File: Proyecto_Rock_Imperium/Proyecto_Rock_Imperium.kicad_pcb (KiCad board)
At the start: 2 copper layers, 53.3 x 58.4 mm, 19 parts, among them Q1 2N3904, Q2 2N3904

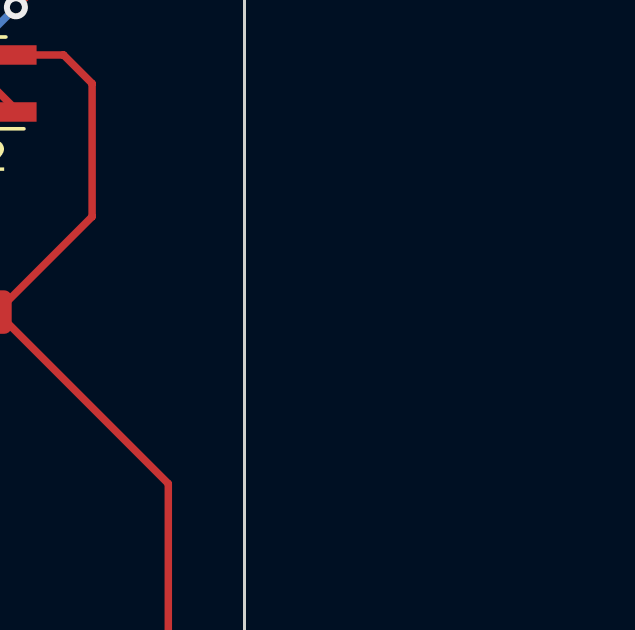
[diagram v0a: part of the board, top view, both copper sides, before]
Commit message: Actualizado esquema y añadido switch
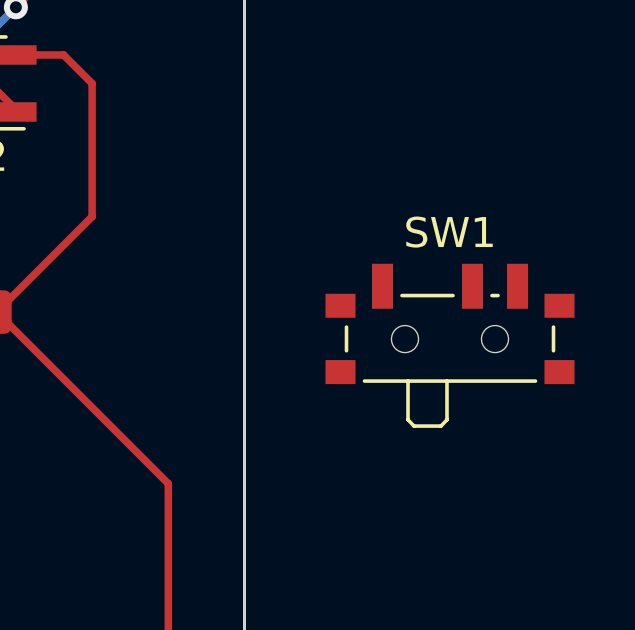
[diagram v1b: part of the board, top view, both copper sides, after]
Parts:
- added SW1: SW_SPDT, Button_Switch_SMD:SW_SPDT_PCM12, F.Cu at (171.9, 76.8)
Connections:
- net Net-(BT1--) renamed GND
- net Net-(D1-A) renamed /leds_b
- net Net-(D1-K) renamed /k_b
- net Net-(D4-A) renamed /leds_a
- net Net-(D4-K) renamed /k_a
- net Net-(Q1-B) renamed /chr_a
- net Net-(Q2-B) renamed /chr_b
- BT1 pad 1: Net-(BT1-+) -> +3V0
- R1 pad 1: Net-(BT1-+) -> /sw_on
- R2 pad 1: Net-(BT1-+) -> /sw_on
- R3 pad 1: Net-(BT1-+) -> /sw_on
- R4 pad 1: Net-(BT1-+) -> /sw_on
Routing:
- net Net-(BT1-+): track 99.8 -> 0.00 mm, vias 2 -> 0
- net (no net): track 0.00 -> 99.8 mm, vias 0 -> 2

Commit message: terminado a falta de revision
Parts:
- removed Ref**: Val**, proyecto_rock:RoCkImPeRiUm
- removed Ref**: Val**, proyecto_rock:IEEE2
- removed Ref**: Val**, proyecto_rock:UPCT2
- removed Ref**: Val**, proyecto_rock:UPCT
- added REF**: TestPoint_Pad_D4.0mm, TestPoint:TestPoint_Pad_D4.0mm, B.Cu at (156.0, 78.5)
- BT1, SW1: moved to B.Cu
- moved R3 71.5 mm to (178.5, 102.5), turned to 90 degrees
- moved Q1 70.8 mm to (190.4, 85.2), turned to 0 degrees
- moved BT1 51.8 mm to (155.9, 107.6), turned to 150 degrees
- moved R4 49.9 mm to (124.9, 97.3), turned to 90 degrees
- moved SW1 48.9 mm to (156.3, 123.2), turned to 180 degrees
- moved R2 42.8 mm to (172.0, 96.4), turned to 180 degrees
- moved D3 42.8 mm to (155.9, 116.1), turned to 0 degrees
- moved D4 42.0 mm to (166.2, 91.1)
- moved C1 39.6 mm to (190.0, 96.4), turned to 180 degrees
- moved D2 35.5 mm to (172.6, 82.1), turned to 180 degrees
- moved Q2 34.9 mm to (123.7, 81.2)
- moved R1 30.8 mm to (130.5, 97.4), turned to 90 degrees
- moved D1 22.8 mm to (140.9, 90.3)
- moved D6 22.3 mm to (172.6, 76.8), turned to 180 degrees
- moved C2 12.6 mm to (126.4, 87.5), turned to -90 degrees
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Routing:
- net (no net): track 99.8 -> 0.00 mm, vias 2 -> 0
- net /sw_on: track 0.00 -> 96.6 mm, vias 0 -> 2
- net /k_b: track 37.3 -> 111.2 mm, vias 0 -> 4
- net /chr_a: track 56.4 -> 122.4 mm
- net /leds_b: track 26.7 -> 80.1 mm, vias 0 -> 5
- net /chr_b: track 120.2 -> 75.4 mm, vias 0 -> 2
- net +3V0: track 0.00 -> 39.6 mm
- net /leds_a: track 26.7 -> 48.0 mm, vias 0 -> 4
- net /k_a: track 56.9 -> 73.6 mm, vias 2 -> 5
- net GND: track 44.6 -> 42.1 mm, vias 2 -> 1
- added copper zone on B.Cu, net GND
- added copper zone on F.Cu, net GND
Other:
- board size 53.3 x 58.4 mm -> 82.1 x 66.2 mm

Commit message: terminado. Pendiente revision y pulir bateria
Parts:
- moved C1 11.3 mm to (182.1, 88.3)
- moved C2 11.3 mm to (118.6, 79.4)
- moved D3 11.3 mm to (148.1, 108.0)
- moved D4 11.3 mm to (158.4, 83.0)
- moved Q1 11.3 mm to (182.6, 77.1)
- moved Q2 11.3 mm to (115.8, 73.0)
- moved R1 11.3 mm to (122.6, 89.3)
- moved R2 11.3 mm to (164.1, 88.3)
- moved R4 11.3 mm to (117.1, 89.1)
- moved D1 11.3 mm to (133.1, 82.2)
- moved D5 11.3 mm to (138.4, 82.2)
- moved BT1 11.3 mm to (148.0, 99.5)
- moved R3 11.3 mm to (170.6, 94.4)
- moved REF** 11.3 mm to (148.1, 70.3)
- moved D2 11.3 mm to (164.7, 73.9)
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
